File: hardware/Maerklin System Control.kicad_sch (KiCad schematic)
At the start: 20 parts, among them J1 Female Header, J2 Output, J3 Input, J4 Conn_S3 Mini, SW1 UP, SW2 RIGHT, SW3 DOWN, SW4 LEFT, SW5 SELECT, SW6 BACK

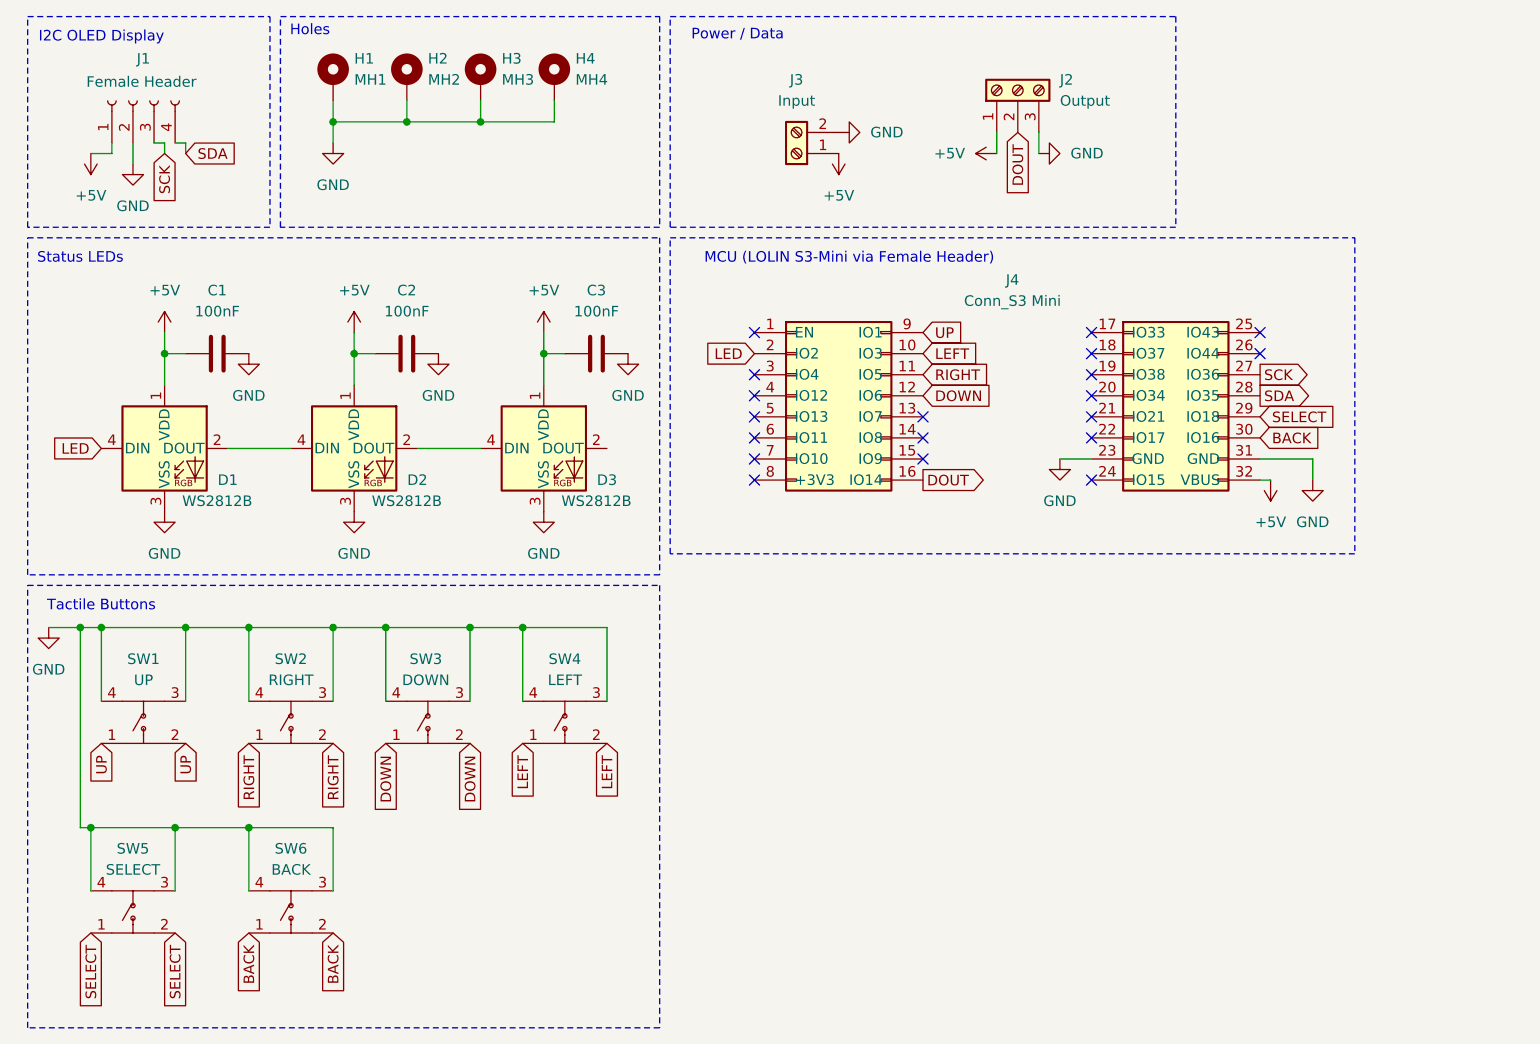
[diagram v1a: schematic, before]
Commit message: switch from global net labels to local
Signed-off-by: Peter Siegmund <developer@mars3142.org>
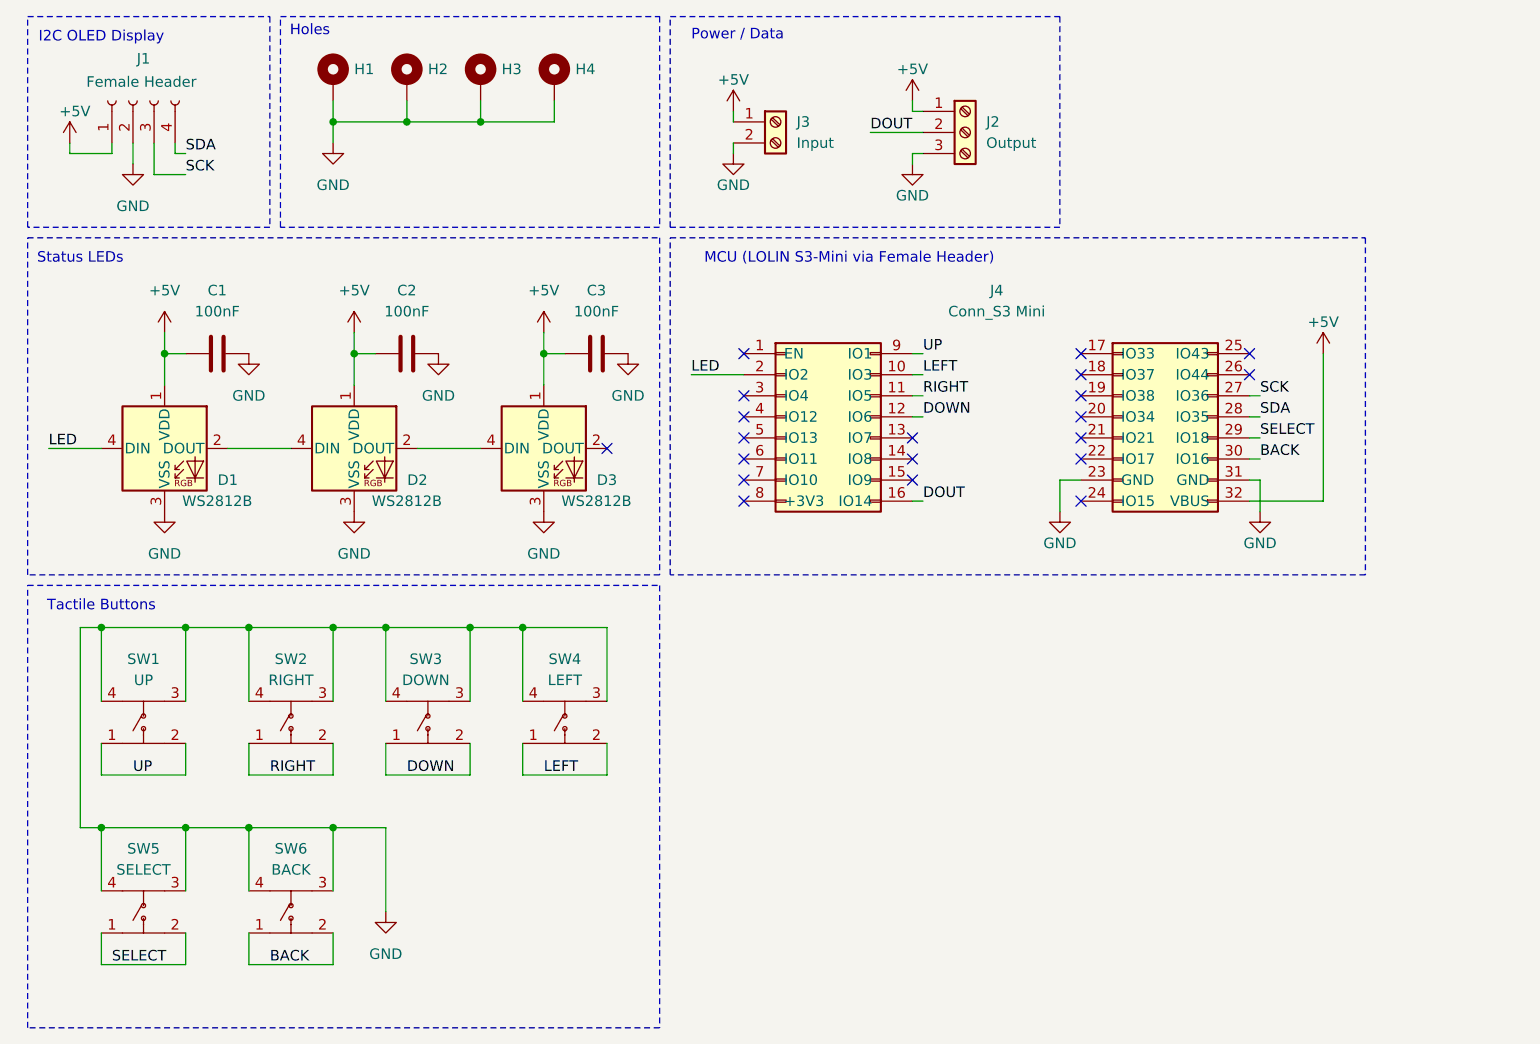
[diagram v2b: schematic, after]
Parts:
- J1: footprint Connector_PinSocket_2.54mm:PinSocket_1x04_P2.54mm_Vertical -> Connector_PinSocket_2.54mm:PinSocket_1x04_P2.54mm_Horizontal
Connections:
- no-connect marks 19 -> 20
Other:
- moved on the sheet: J2, J3, J4, SW5

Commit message: ESP32 C6 support
Signed-off-by: Peter Siegmund <developer@mars3142.org>
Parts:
- removed J4: Conn_S3 Mini, wemos:PinSocket_S3 Mini, symbol wemos:Conn_S3 Mini
- added R1: 220Ω, Resistor_SMD:R_0805_2012Metric_Pad1.20x1.40mm_HandSolder, symbol Device:R
- added R2, R3: 4,7 kΩ, Resistor_SMD:R_0805_2012Metric_Pad1.20x1.40mm_HandSolder, symbol Device:R
- added U1: XIAO-ESP32-C6-DIP, Seeed_Studio_XIAO_Series:XIAO-ESP32-C6-DIP, symbol Seeed_Studio_XIAO_Series:XIAO-ESP32-C6-DIP
- renumbered J3 to J2, J2 to J3
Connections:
- net +5V: now also U1.14 (VBUS)
- net BACK: now also U1.3 (GPIO2_A2_D2)
- net DOUT: now also R1.1
- net DOWN: now also U1.8 (GPIO17_D7_RX)
- net GND: now also U1.13 (GND)
- net LED: now also U1.7 (GPIO16_D6_TX)
- net LEFT: now also U1.10 (GPIO20_D9_MISO)
- net RIGHT: now also U1.9 (GPIO19_D8_SCK)
- net SCK: now also R3.1, U1.6 (GPIO23_D5_SCL)
- net SDA: now also R2.1, U1.5 (GPIO22_D4_SDA)
- net SELECT: now also U1.2 (GPIO1_A1_D1)
- net UP: now also U1.11 (GPIO18_D10_MOSI)
- new net: R1.2, U1.4 (GPIO21_D3)
- new net +3V3: R2.2, R3.2, U1.12 (3V3)
- no-connect marks 20 -> 2
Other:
- note added: "MCU (via Female Header)"
- note removed: "MCU (LOLIN S3-Mini via Female Header)"

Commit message: latest KiCad format
Signed-off-by: Peter Siegmund <developer@mars3142.org>
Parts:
- removed J2: Input, TerminalBlock_Phoenix:TerminalBlock_Phoenix_MKDS-1,5-2_1x02_P5.00mm_Horizontal, symbol Connector:Screw_Terminal_01x02
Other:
- moved on the sheet: J3
